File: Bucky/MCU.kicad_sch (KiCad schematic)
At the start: 35 parts, among them J15 502585-0470, J16 FTSH-105-01-F-D-RA-K, J202 Conn_Picoblade_JST_DEBUG, J403 USB4105-GF-A, U401 STM32G483RET6, Y201 ABM8W-48.0000MHZ-4-D1X-T3

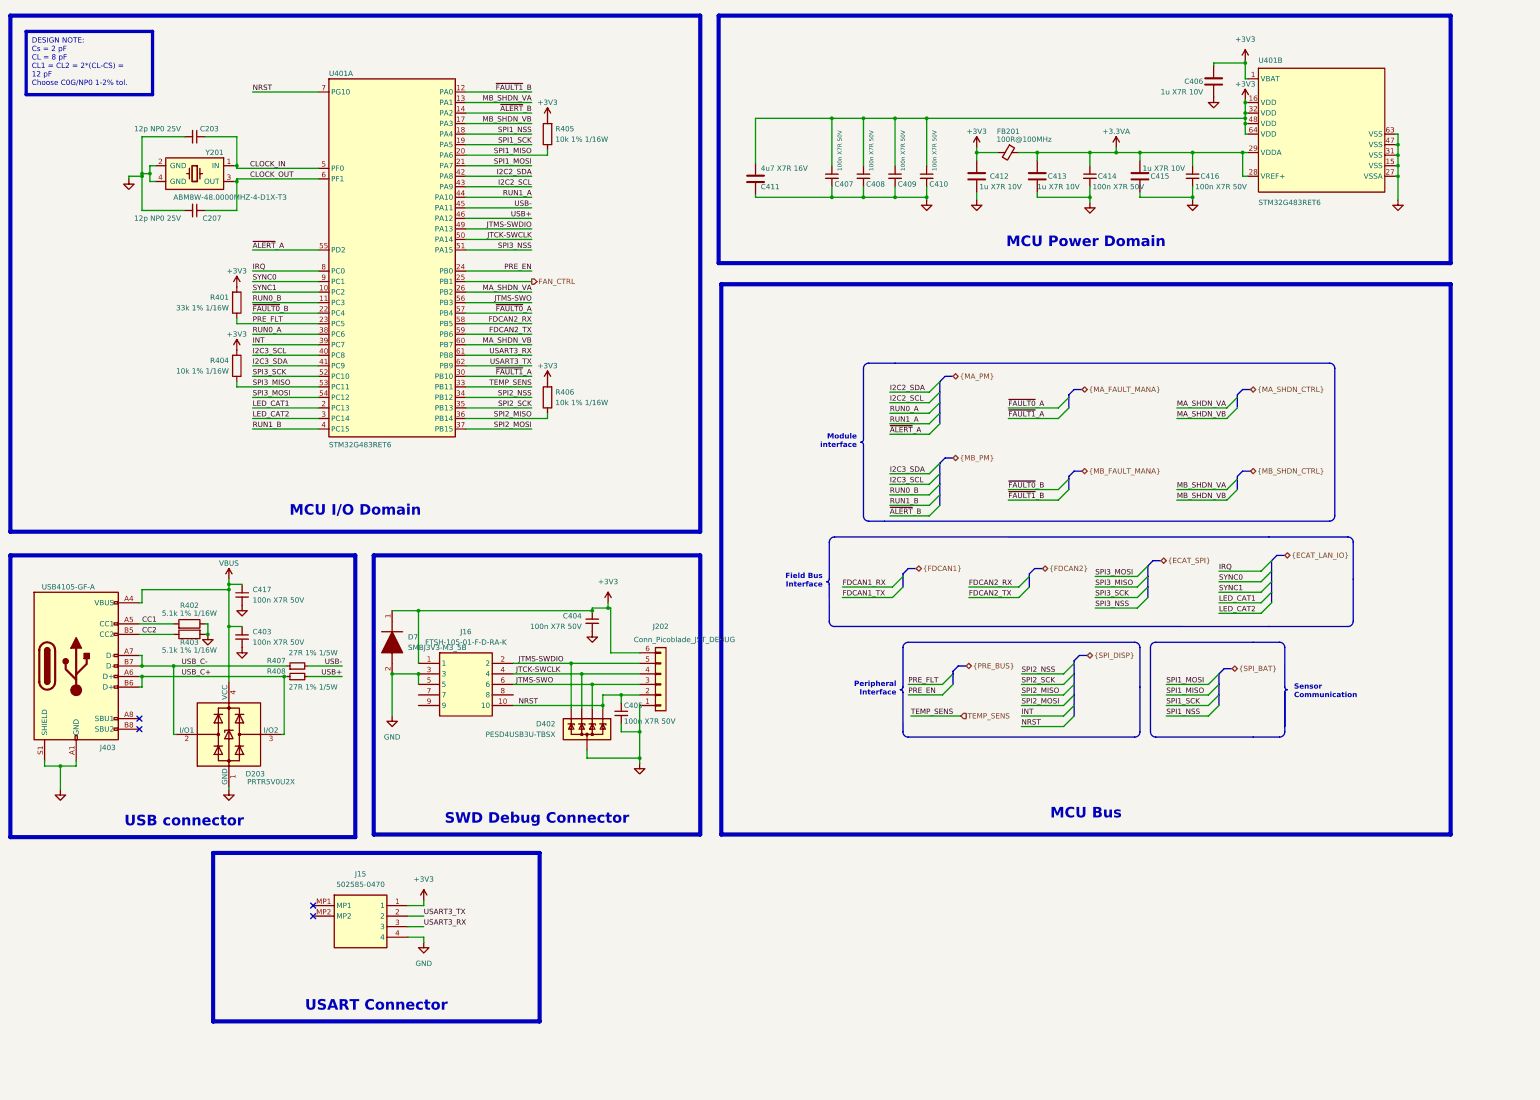
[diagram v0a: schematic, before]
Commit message: adapted schematics and added more protection from GEODE (Reverse Current)
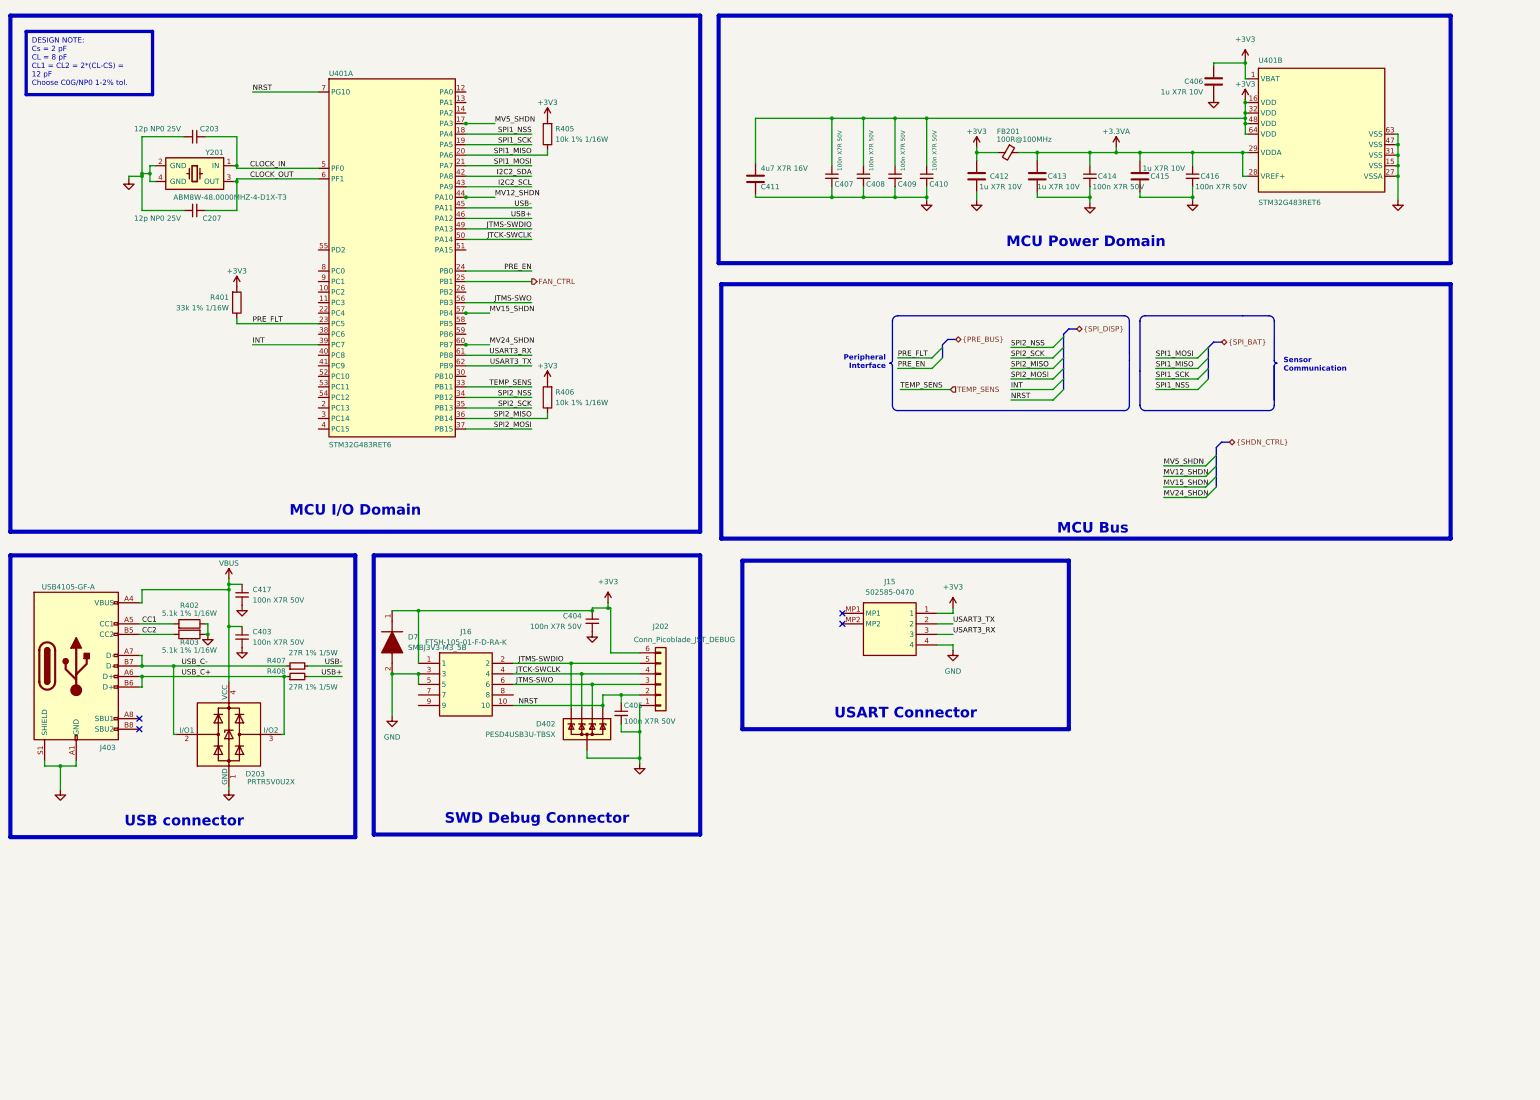
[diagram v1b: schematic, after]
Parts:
- removed R404: 10k 1% 1/16W, 0_resistor_smd:R_0402_1005_DensityHigh, symbol Device:R
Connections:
- net FDCAN2_RX: no longer names the net of U401.58 (PB5)
- net FDCAN2_TX: no longer names the net of U401.59 (PB6)
- net I2C3_SCL: no longer names the net of U401.40 (PC8)
- net I2C3_SDA: no longer names the net of U401.41 (PC9)
- net IRQ: no longer names the net of U401.8 (PC0)
- net LED_CAT1: no longer names the net of U401.2 (PC13)
- net LED_CAT2: no longer names the net of U401.3 (PC14)
- net MA_SHDN_VA: no longer names the net of U401.26 (PB2)
- net MA_SHDN_VB renamed MV24_SHDN
- net MB_SHDN_VA: no longer names the net of U401.13 (PA1)
- net MB_SHDN_VB renamed MV5_SHDN
- net RUN0_A: no longer names the net of U401.38 (PC6)
- net RUN0_B: no longer names the net of U401.11 (PC3)
- net RUN1_A renamed MV12_SHDN
- net RUN1_B: no longer names the net of U401.4 (PC15)
- net SPI3_MISO: no longer names the net of U401.53 (PC11)
- net SPI3_MOSI: no longer names the net of U401.54 (PC12)
- net SPI3_NSS: no longer names the net of U401.51 (PA15)
- net SPI3_SCK: no longer names the net of U401.52 (PC10)
- net SYNC0: no longer names the net of U401.9 (PC1)
- net SYNC1: no longer names the net of U401.10 (PC2)
- net ~{ALERT}_A: no longer names the net of U401.55 (PD2)
- net ~{ALERT}_B: no longer names the net of U401.14 (PA2)
- net ~{FAULT0}_A renamed MV15_SHDN
- net ~{FAULT0}_B: no longer names the net of U401.22 (PC4)
- net ~{FAULT1}_A: no longer names the net of U401.30 (PB10)
- net ~{FAULT1}_B: no longer names the net of U401.12 (PA0)
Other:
- moved on the sheet: J15

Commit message: upadated scchematics
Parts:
- added C1709, C1801: 100n X7R 50V, 0_capacitor_smd:C_0402_1005_DensityHigh, symbol Device:C_Small
- added C1802: 4.7u X7R 16V, 0_capacitor_smd:C_0603_1608_DensityHigh, symbol Device:C
- added J1702: 505110-3091, 0_connectors:5051103091, symbol 505110-3091:505110-3091
- added J1801: S2B-PH-SM4-TB, 0_connectors:JST_PH_S2B-PH-SM4-TB_1x02-1MP_P2.00mm_Horizontal, symbol Connector:Screw_Terminal_01x02
- added Q1401: PMV90ENER, 0_package_SOT_TO_SMD:SOT-23-3, symbol Simulation_SPICE:NMOS
- added U1801: DGD0216WT-7, Package_TO_SOT_SMD:TSOT-23-5, symbol 0_gate_driver:DGD0216WT-7
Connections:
- net GND: now also C1709.2, C1801.2, C1802.2, J1702.1, J1702.11, J1702.13, J1702.17, J1702.21, J1702.24, J1702.25, J1702.30, J1702.5, J1702.9, Q1401.2 (S), U1801.2 (COM)
- net INT: now also J1702.3
- net NRST: now also J1702.2
- net SPI2_MISO: now also J1702.7
- net SPI2_MOSI: now also J1702.6
- net SPI2_NSS: now also J1702.4
- net SPI2_SCK: now also J1702.8
- net SPI1_NSS0: now reaches U401.40 (PC8)
- net SPI1_NSS1: now reaches U401.41 (PC9)
- net SPI1_NSS2: now reaches U401.52 (PC10)
- net SPI1_NSS3: now reaches U401.53 (PC11)
- net SPI1_NSS4: now reaches U401.54 (PC12)
- net I2C2_SCL: no longer names the net of U401.43 (PA9)
- net I2C2_SDA: no longer names the net of U401.42 (PA8)
- net SPI1_NSS: no longer names the net of U401.18 (PA4)
- new net: J1801.2 (Pin_2), Q1401.3 (D)
- new net: Q1401.1 (G), U1801.4 (OUT)
- new net +12V: J1801.1 (Pin_1)
- new net +5V: C1709.1, C1801.1, C1802.1, J1702.26, J1702.27, U1801.5 (VCC)
- new net APWM: J1702.10
- new net FAN: U1801.3 (IN)
- new net nSHDN: J1702.12
- no-connect marks 4 -> 17
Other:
- moved on the sheet: C406, C407, C408, C409, C410, C411, C412, C413, C414, C415, C416, D7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
